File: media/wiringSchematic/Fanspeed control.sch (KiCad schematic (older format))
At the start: 7 parts, among them J1 16x2B LCD i2c, J2 rotary encoder, J3 Proportional Control Solid St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, J4 SHT31 Temp/Hum Sensor, SW1 Standby Switch

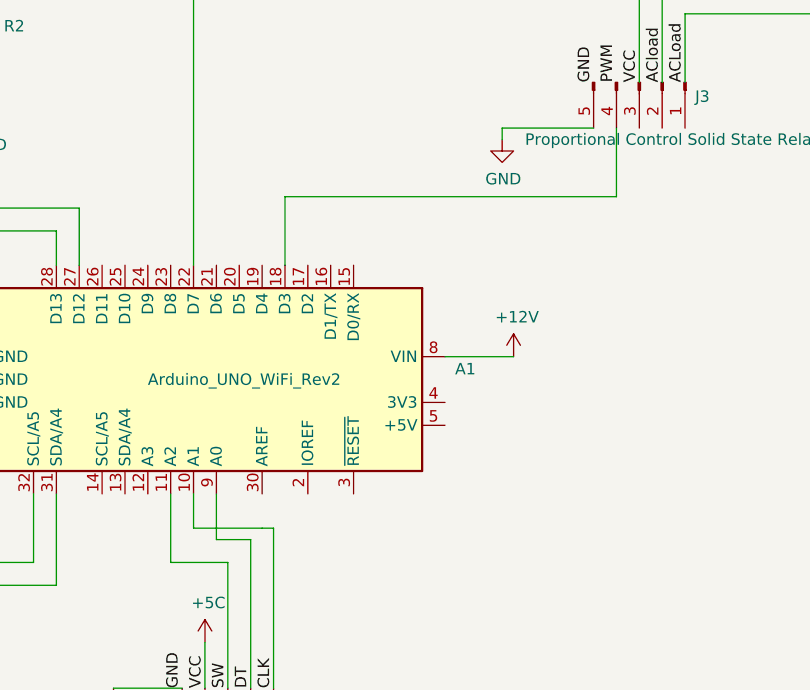
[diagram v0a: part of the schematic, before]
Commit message: added new parts to schymeatic+
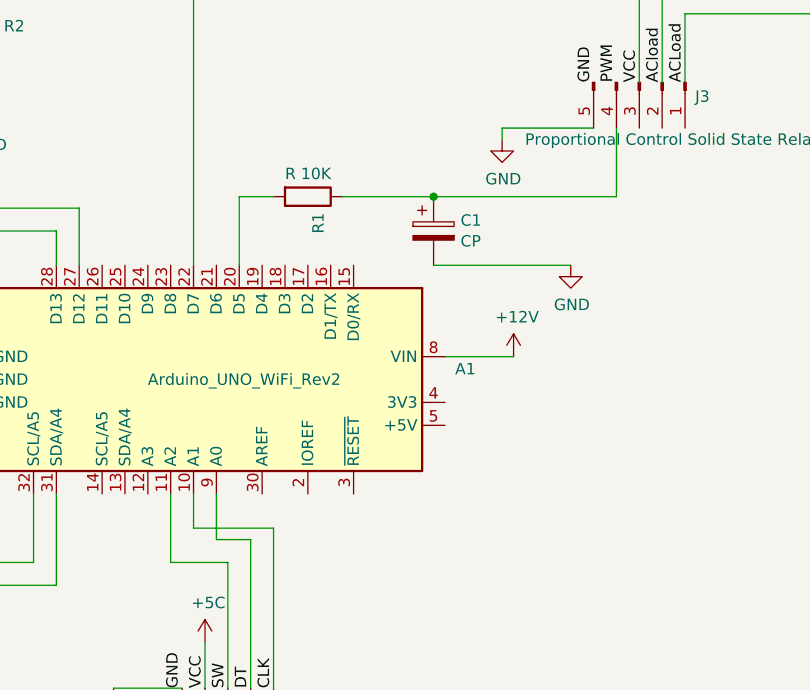
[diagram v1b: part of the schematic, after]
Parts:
- added C1: CP, symbol Device:CP
- added R1: R 10K, symbol Device:R
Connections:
- wire segments 45 -> 47
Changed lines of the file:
@@
 	5500 1950 5500 2250
-Wire Wire Line
-	5500 2250 4050 2250
 Wire Wire Line
 	5600 1750 5600 1200
@@
 	950  2500 950  2400
 Wire Wire Line
-	4050 2250 4050 2550
+	3850 2250 3850 2550
 Wire Wire Line
 	1800 2400 3050 2400
@@
 	4000 4400 4000 3700
 Wire Wire Line
-	4000 3700 3950 3700
-Wire Wire Line
 	3650 3700 3650 3550
 Wire Wire Line
-	3950 3700 3650 3700
+	3650 3700 4000 3700
+$Comp
+L Device:R R1
+U 1 1 611193BD
+P 4150 2250
+F 0 "R1" H 4220 2296 50  0000 L CNN
+F 1 "R 10K" V 4050 2150 50  0000 L CNN
+F 2 "" V 4080 2250 50  0001 C CNN
+F 3 "~" H 4150 2250 50  0001 C CNN
+	1    4150 2250
+	0    1    1    0
+$EndComp
+Wire Wire Line
+	3850 2250 4000 2250
+$Comp
+L Device:CP C1
+U 1 1 6111A6D4
+P 4700 2400
+F 0 "C1" H 4818 2446 50  0000 L CNN
+F 1 "CP" H 4818 2355 50  0000 L CNN
+F 2 "" H 4738 2250 50  0001 C CNN
+F 3 "~" H 4700 2400 50  0001 C CNN
+	1    4700 2400
+	1    0    0    -1
+$EndComp
+Wire Wire Line
+	4300 2250 4700 2250
+Wire Wire Line
+	5500 2250 4700 2250
+Connection ~ 4700 2250
+Wire Wire Line
+	4700 2550 5300 2550
+$Comp
+L power:GND #PWR03
+U 1 1 6111EECC
+P 5300 2550
+F 0 "#PWR03" H 5300 2300 50  0001 C CNN
+F 1 "GND" H 5305 2377 50  0000 C CNN
+F 2 "" H 5300 2550 50  0001 C CNN
+F 3 "" H 5300 2550 50  0001 C CNN
+	1    5300 2550
+	1    0    0    -1
+$EndComp
 $EndSCHEMATC

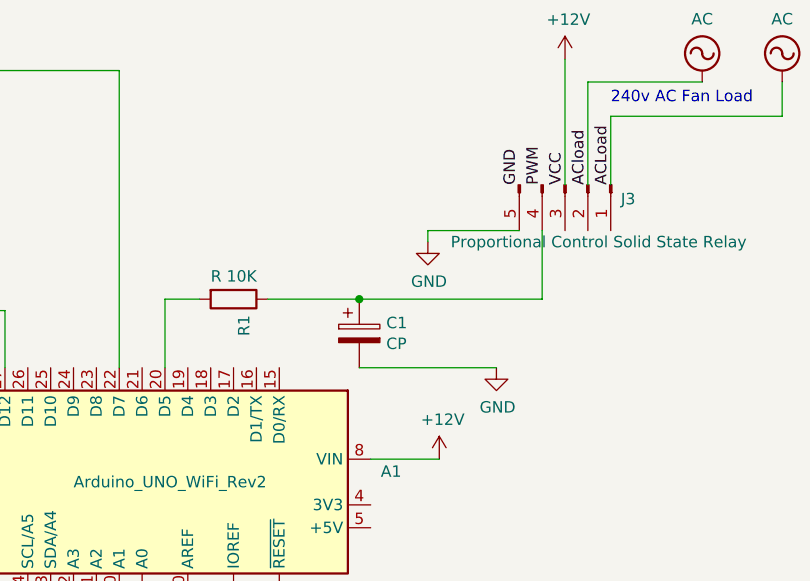
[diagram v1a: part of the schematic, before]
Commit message: added to the readme about pwm and rc filter
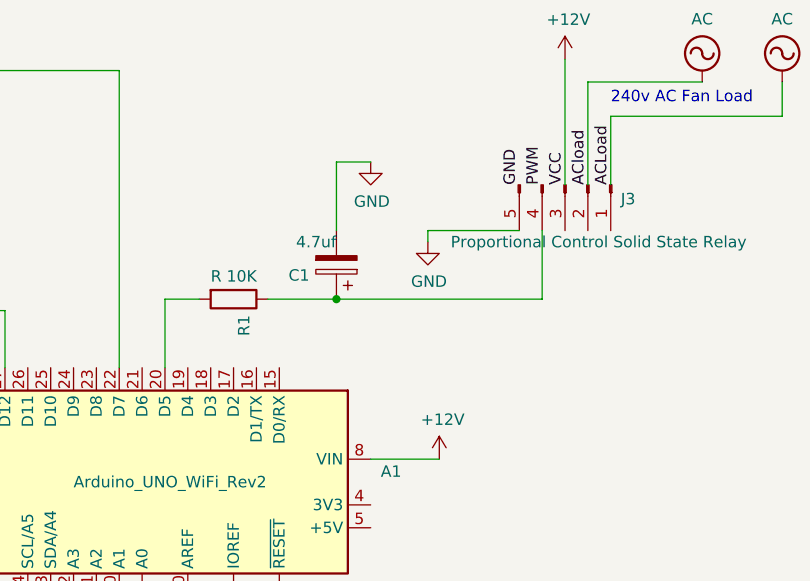
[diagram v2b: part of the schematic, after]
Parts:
- C1: value CP -> 4.7uf
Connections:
- wire segments 47 -> 48
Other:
- moved on the sheet: C1
